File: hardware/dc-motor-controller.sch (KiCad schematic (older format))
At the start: 27 parts, among them IC1 ATMEGA88PA-P, M0 DC_motor, M1 DC_motor, M2 DC_motor, P1 Power connector, P2 ISP interface, SW0-0 SW_PUSH, SW0-1 SW_PUSH, SW1-0 SW_PUSH, SW1-1 SW_PUSH, SW2-0 SW_PUSH, SW2-1 SW_PUSH, U0 BA6956AN, U1 BA6956AN, U2 BA6956AN, U3 7805

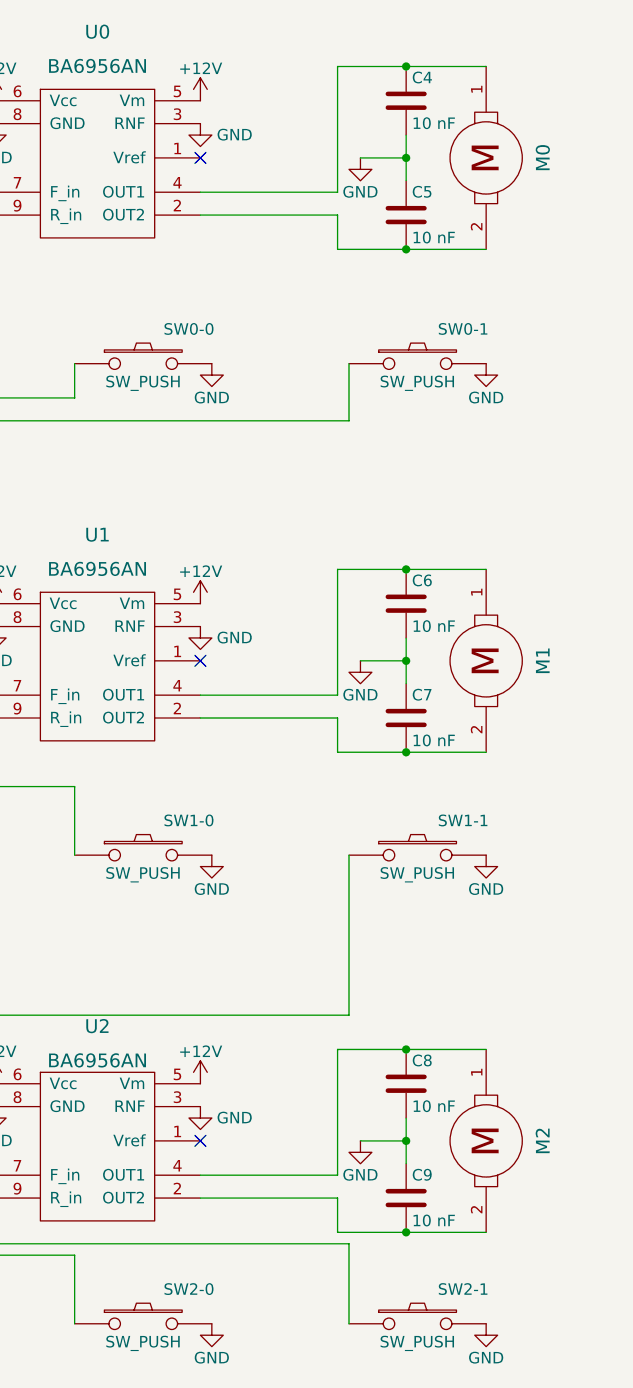
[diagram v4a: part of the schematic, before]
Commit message: Add trimmers for analog voltage control to schematic
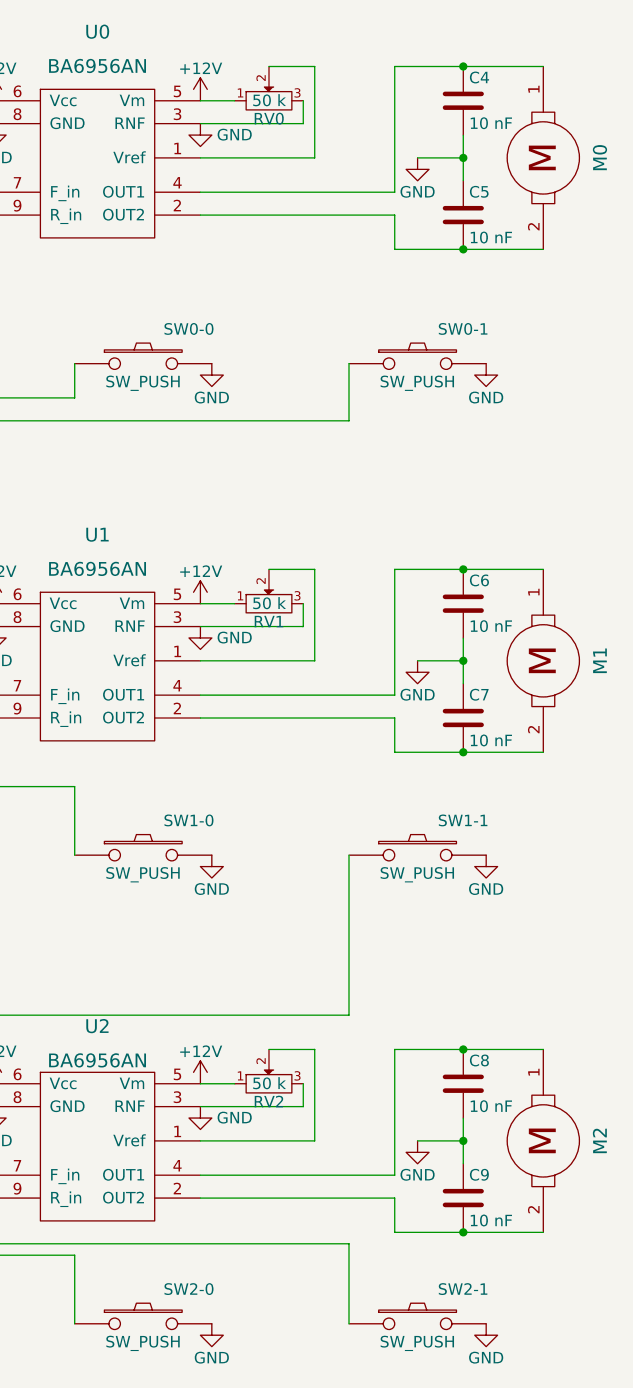
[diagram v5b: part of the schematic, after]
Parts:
- added RV0, RV1, RV2: 50 k, symbol POT
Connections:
- net +12V: now also RV0.1, RV1.1, RV2.1
- net GND: now also RV0.3, RV1.3, RV2.3
- net at U0.1 (Vref): now also RV0.2
- net at U1.1 (Vref): now also RV1.2
- net at U2.1 (Vref): now also RV2.2
- no-connect marks 11 -> 8
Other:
- moved on the sheet: C4, C5, C6, C7, C8, C9, M0, M1, M2
